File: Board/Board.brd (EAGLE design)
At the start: 100 x 60 mm, 96 parts, among them Q1 SP0503BAHTG

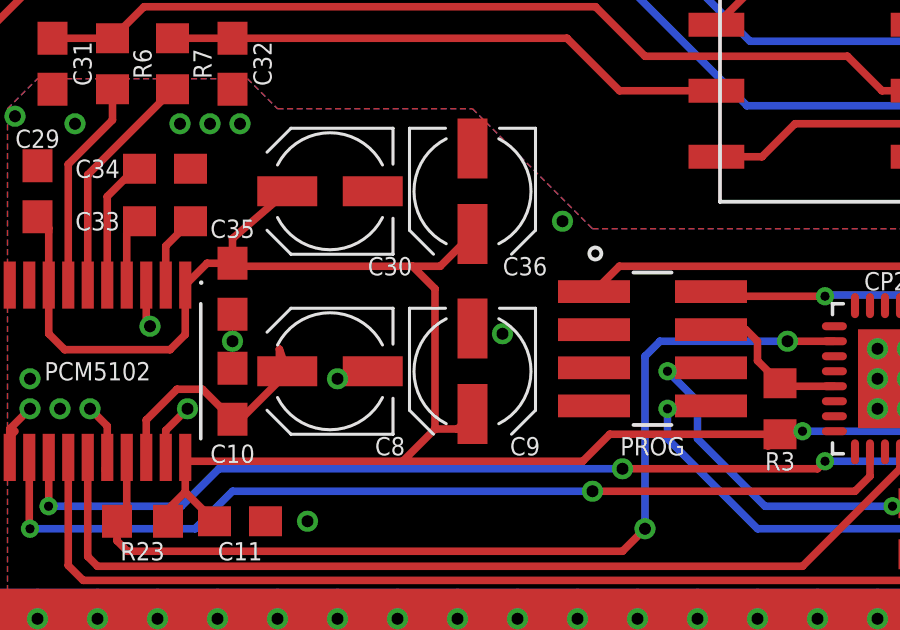
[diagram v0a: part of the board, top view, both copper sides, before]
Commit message: fixed bad via location
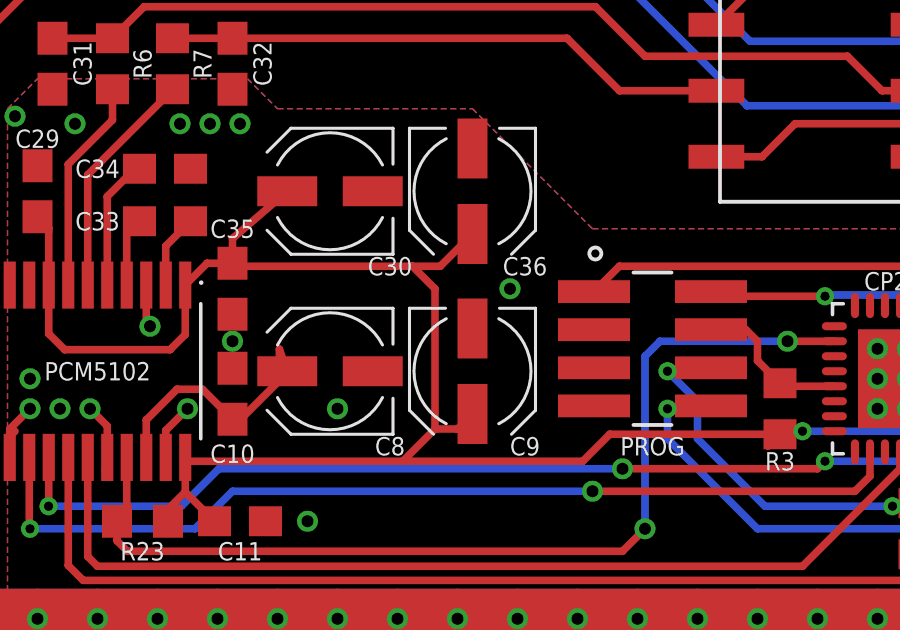
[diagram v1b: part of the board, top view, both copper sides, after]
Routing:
- net GND: vias 156 -> 155
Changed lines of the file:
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@@
 <via x="54.75" y="17.5" extent="1-16" drill="0.4" shape="octagon"/>
 <via x="55.75" y="17.5" extent="1-16" drill="0.4" shape="octagon"/>
-<via x="66.5" y="14.25" extent="1-16" drill="0.4" shape="octagon"/>
-<via x="64.5" y="10.5" extent="1-16" drill="0.4" shape="octagon"/>
+<via x="64.75" y="12" extent="1-16" drill="0.4" shape="octagon"/>
 <via x="41" y="34" extent="1-16" drill="0.4" shape="octagon"/>
 <via x="40" y="34" extent="1-16" drill="0.4" shape="octagon"/>
@@
 <wire x1="66" y1="26" x2="65.25" y2="26" width="0.254" layer="16"/>
 <wire x1="92.62" y1="10.75" x2="91.5" y2="10.75" width="0.254" layer="1"/>
-<via x="59" y="9" extent="1-16" drill="0.4" shape="octagon"/>
+<via x="59" y="8" extent="1-16" drill="0.4" shape="octagon"/>
 <via x="86.75" y="12.75" extent="1-16" drill="0.4" shape="octagon"/>
 <via x="87.75" y="12.75" extent="1-16" drill="0.4" shape="octagon"/>

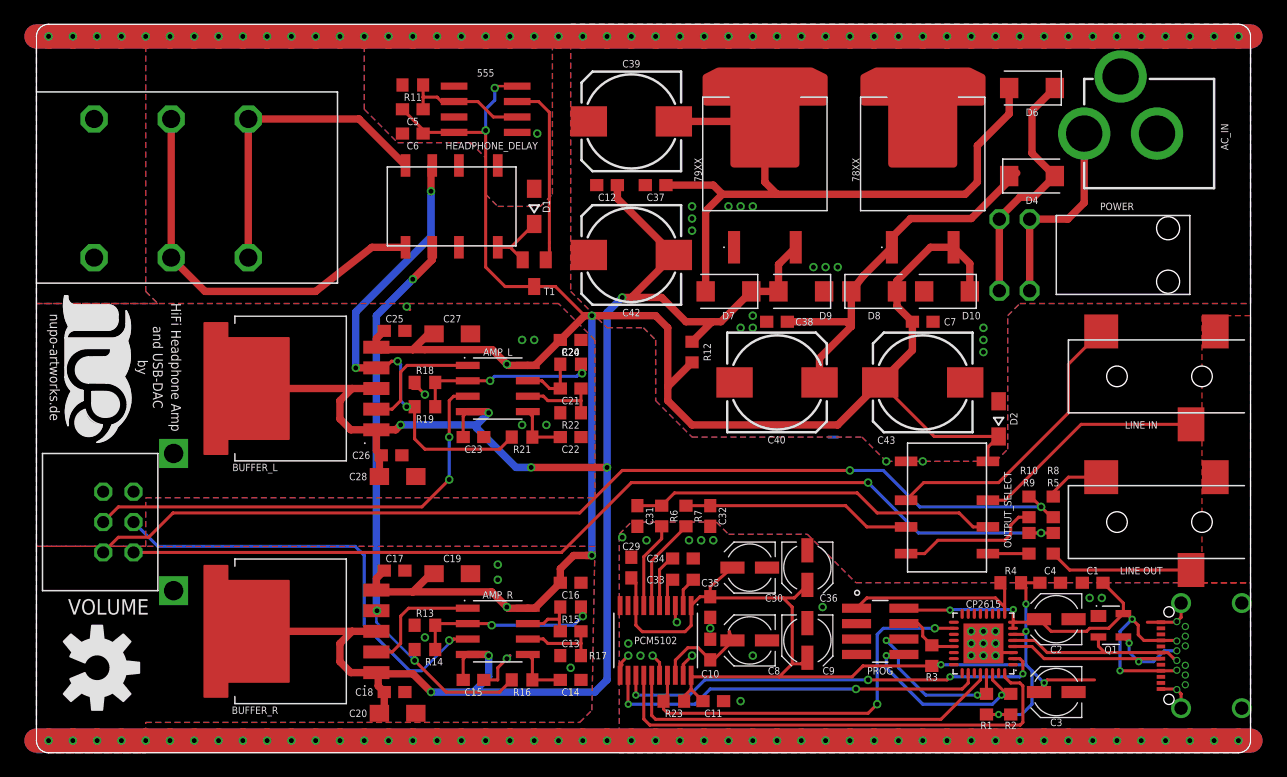
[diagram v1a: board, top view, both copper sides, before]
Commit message: updated relay orientation
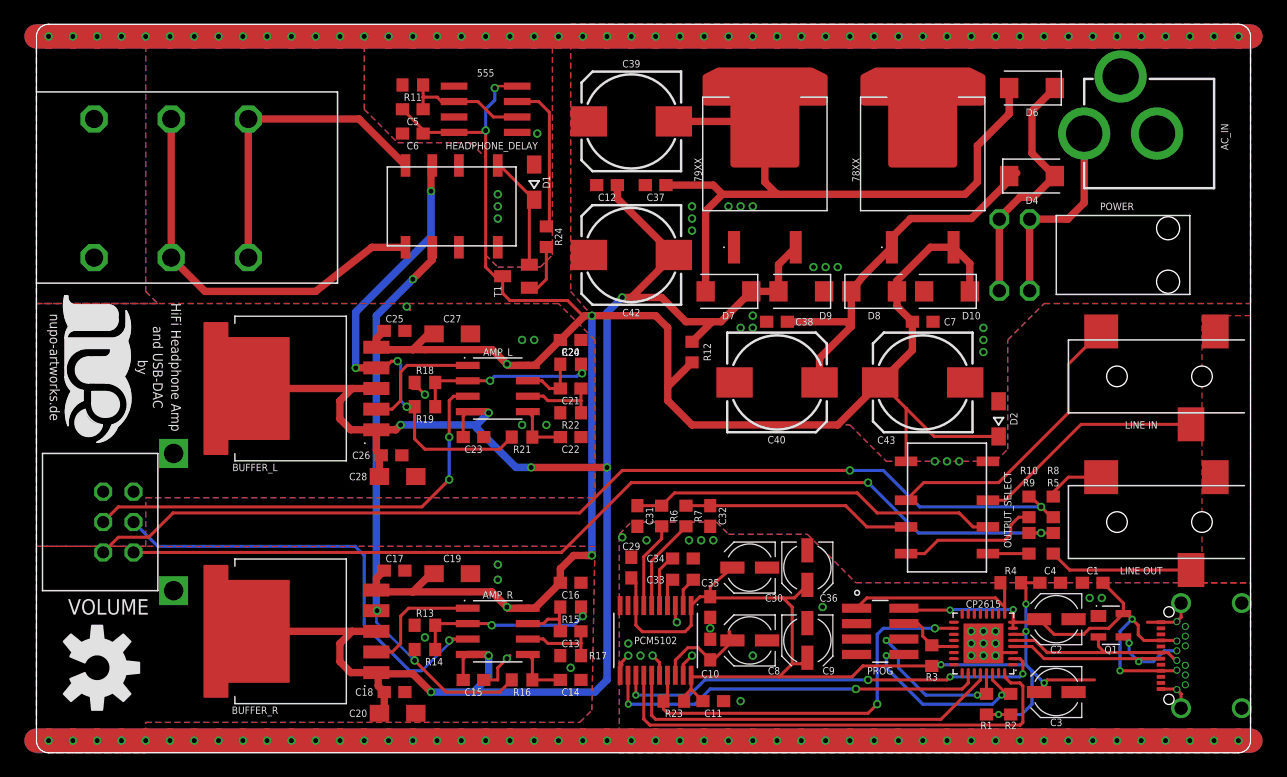
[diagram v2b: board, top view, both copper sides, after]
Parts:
- added R24: 100, rcl:R0603
- moved D1 2.00 mm to (41.0, 47.0)
- moved T1 1.52 mm to (39.5, 39.2), turned to 90 degrees
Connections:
- new net N$43: R24.2, T1.B
- net GND: now also HEADPHONE_DELAY.1, OUTPUT_SELECT.1; no longer HEADPHONE_DELAY.8, OUTPUT_SELECT.8
- net N$42: now also R24.1; no longer T1.B
- net N$44: now also HEADPHONE_DELAY.8; no longer HEADPHONE_DELAY.1
- net V+: now also OUTPUT_SELECT.8; no longer OUTPUT_SELECT.1
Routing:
- net N$43: track 0.00 -> 4.96 mm
- net N$44: track 5.25 -> 9.68 mm
- net N$42: track 15.3 -> 12.5 mm
- net V+: track 174.8 -> 177.6 mm
- net GND: track 427.2 -> 426.4 mm, vias 155 -> 159
